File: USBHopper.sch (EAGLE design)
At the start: 38 parts, among them X1 USB-1X-2S-PLUG-A-SMD

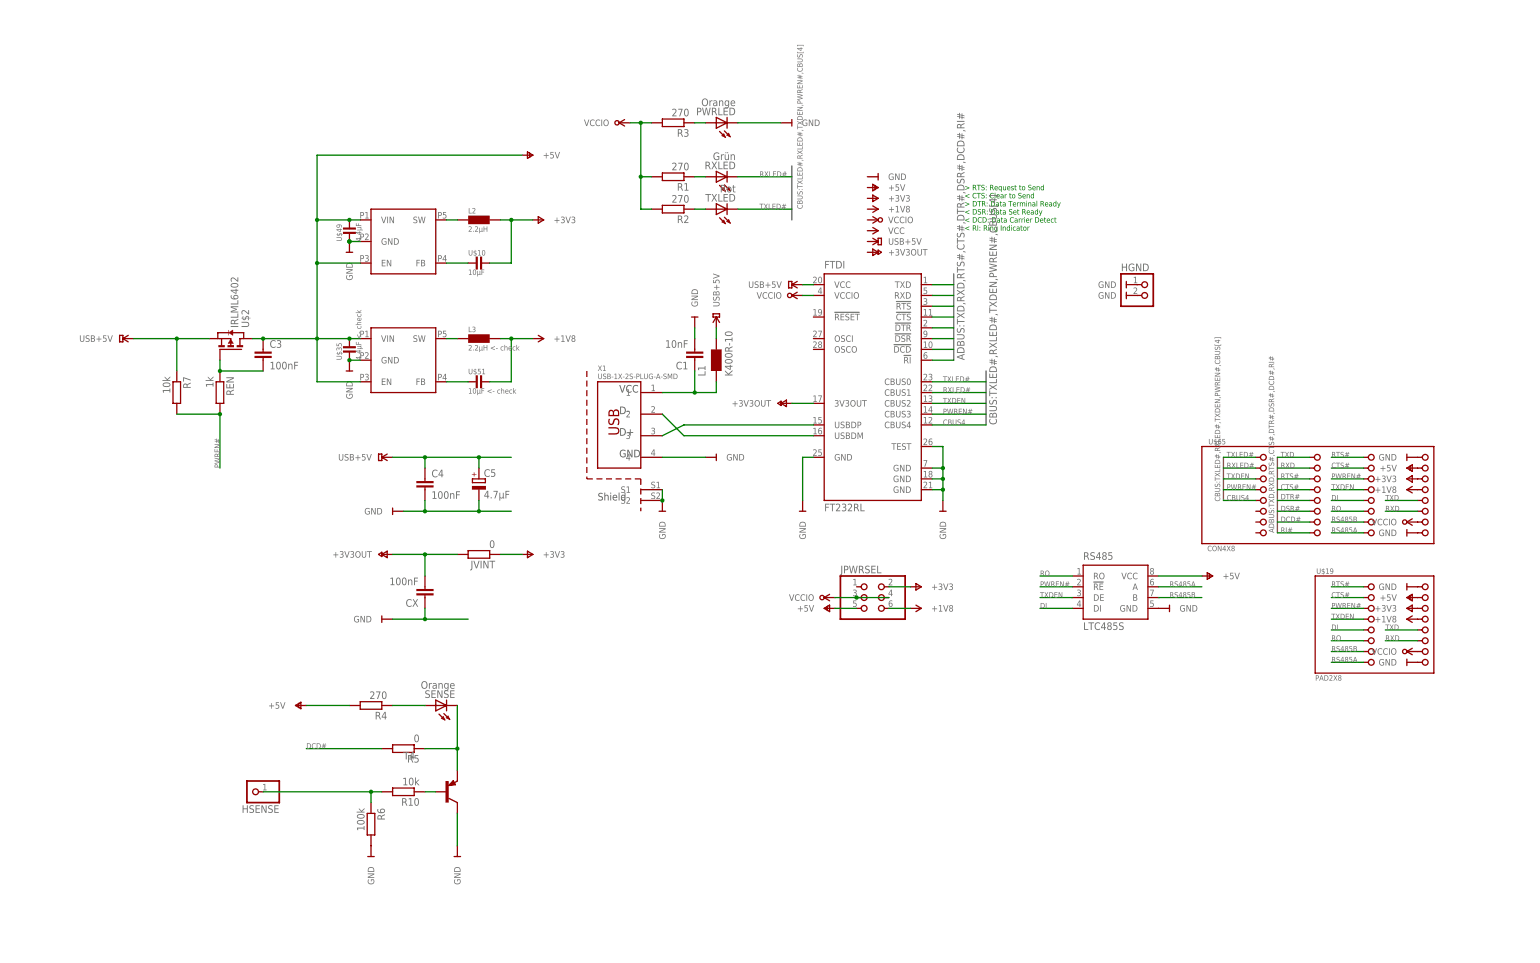
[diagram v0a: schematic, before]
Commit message: LED Steuerung via RN4904
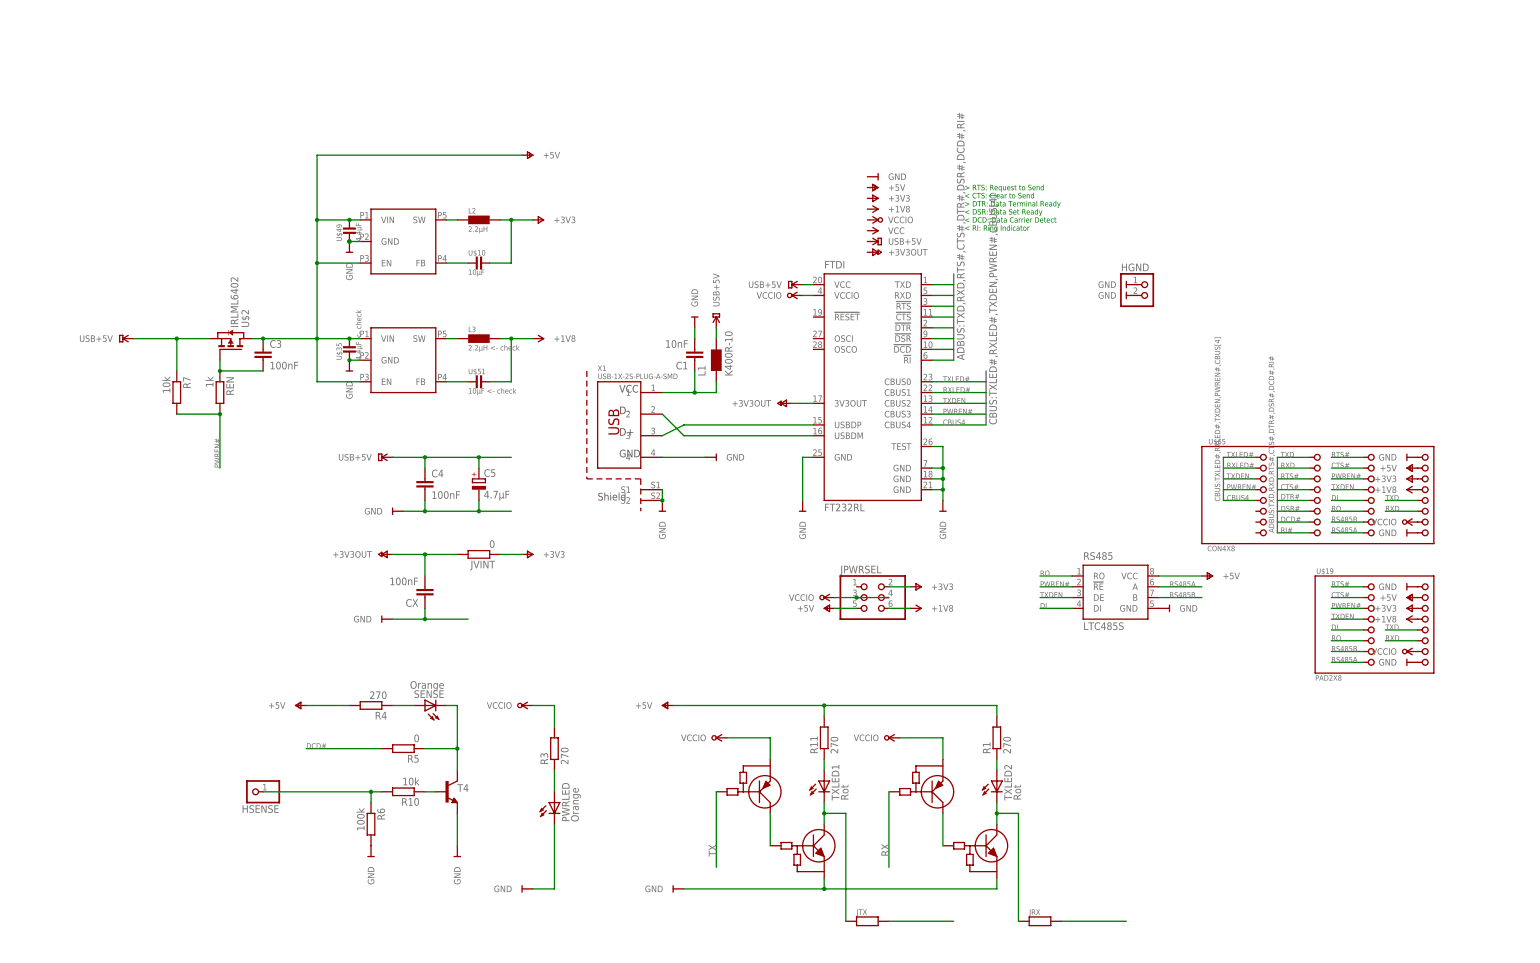
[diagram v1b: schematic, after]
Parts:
- removed R2: 270, rcl:R-EU_R0805
- removed RXLED: Grün, led:LEDCHIP-LED0805
- removed TXLED: Rot, led:LEDCHIP-LED0805
- added JRX, JTX: (no value), flo-parts:RESISTORCONNECT
- added R11: 270, rcl:R-EU_R0805
- added TXLED1, TXLED2: Rot, led:LEDCHIP-LED0805
- added U$32, U$46: (no value), flo-logic:RN4904
- T4: device transistor:BC857A-PNP-SOT23-BEC -> transistor:-NPN-SOT23-EBC
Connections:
- new net N$10: JTX.P$1, TXLED1.C, U$32NPN.E
- new net N$11: R11.1, TXLED1.A
- new net N$12: R1.1, TXLED2.A
- new net N$9: U$32NPN.B, U$32PNP.C
- new net RX: U$46PNP.B
- new net TX: U$32PNP.B
- net +5V: now also R1.2, R11.2
- net GND: now also T4.E, U$32NPN.C, U$46NPN.C; no longer T4.C
- net N$5: now also U$46NPN.B, U$46PNP.C; no longer R1.1, RXLED.A
- net N$6: now also JRX.P$1, TXLED2.C, U$46NPN.E; no longer R2.1, TXLED.A
- net RXLED#: now also JRX.P$2; no longer RXLED.C
- net SENSLED: now also T4.C; no longer T4.E
- net TXLED#: now also JTX.P$2; no longer TXLED.C
- net VCCIO: now also U$32PNP.E, U$46PNP.E; no longer R1.2, R2.2
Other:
- note added: "SIMPLE"
- note added: "integrated"
- moved on the sheet: PWRLED, R1, R3, SENSE

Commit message: pnp/npn package groesser. strom schaltung gefummele.
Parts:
- removed JVINT: 0, rcl:R-EU_R0805
- removed R10: 10k, rcl:R-EU_R0805
- removed R6: 100k, rcl:R-EU_R0805
- removed T4: (no value), transistor:-NPN-SOT23-EBC
- removed U$2: IRLML6402, IRLML6402:IRLML6402
- added IC1: (no value), ic-package:DIL8
- added JINT: (no value), flo-parts:RESISTORCONNECT
- added U$57: DMP2240UDM, flo-logic:DMP2240UDM
- added U$64, U$72: 4k7/47k, flo-logic:PNP_NPN_BIASNXP_PIMD3
- added U$73: (no value), flo-logic:PNP_NPN_BIASNXP_PIMD3
- U$32, U$46: value (none) -> CON1X4; device flo-logic:RN4904 -> flo-header:CON1X4
- renumbered TXLED1 to TXLED, TXLED2 to RXLED
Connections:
- removed net N$23: R10.1, T4.B
- net +3V3: now also JINT.P$2; no longer JVINT.1
- net +3V3OUT: now also JINT.P$1; no longer JVINT.2
- net +5V: now also U$32.P$1, U$57A.D; no longer U$2.D, U$20.EN, U$20.VIN, U$49.P$2
- net DI: now also U$46.P$4
- net GND: now also U$32.P$4, U$64NPN.C, U$72NPN.C, U$73NPN.C; no longer R6.2, T4.E, U$32NPN.C, U$46NPN.C
- net N$10: now also U$64NPN.E; no longer U$32NPN.E
- net N$5: now also U$72NPN.B, U$72PNP.C; no longer U$46NPN.B, U$46PNP.C
- net N$6: now also U$72NPN.E; no longer U$46NPN.E
- net N$9: now also U$64NPN.B, U$64PNP.C; no longer U$32NPN.B, U$32PNP.C
- net PWREN: now also U$57A.G; no longer U$2.G
- net PWREN#: now also U$46.P$2
- net RO: now also U$46.P$1
- net RS485A: now also U$32.P$2
- net RS485B: now also U$32.P$3
- net RX: now also U$72PNP.B; no longer U$46PNP.B
- net SENSE: now also U$73NPN.B; no longer R10.2, R6.1
- net SENSLED: now also U$73NPN.E; no longer T4.C
- net TX: now also U$64PNP.B; no longer U$32PNP.B
- net TXDEN: now also U$46.P$3
- net USB+5V: now also U$20.EN, U$20.VIN, U$49.P$2, U$57A.S; no longer U$2.S
- net VCCIO: now also U$64PNP.E, U$72PNP.E; no longer U$32PNP.E, U$46PNP.E
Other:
- moved on the sheet: C3, PWRLED, R3, R7, REN

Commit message: weiter pwren, leds...
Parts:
- removed IC1: (no value), ic-package:DIL8
- removed JINT: (no value), flo-parts:RESISTORCONNECT
- removed R5: 0, rcl:R-EU_R0805
- added JP1, JP2: (no value), pinhead:PINHD-1X1
- C5: device rcl:CPOL-EUB -> rcl:CPOL-EU153CLV-0405
- PWRLED: value Orange -> Blue
- RXLED: value Rot -> Red
- TXLED: value Rot -> Green
- renumbered R1 to RRX, R11 to RTX, U$64 to UTX, U$72 to URX
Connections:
- new net N$13: R3.2, U$73PNP.C
- new net N$14: JP1.1, U$73PNP.B
- net +3V3: no longer JINT.P$2
- net +3V3OUT: now also JPWRSEL.1; no longer JINT.P$1
- net +5V: now also U$20.EN, U$20.VIN, U$49.P$2
- net DCD#: no longer R5.2
- net PWREN#: now also JP2.1
- net SENSLED: no longer R5.1
- net USB+5V: now also U$73PNP.E; no longer U$20.EN, U$20.VIN, U$49.P$2
- net VCCIO: no longer R3.2
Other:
- note removed: "SIMPLE"
- note removed: "integrated"
- moved on the sheet: HSENSE, PWRLED, R3, R4, SENSE, U$73NPN

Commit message: +5V->USB+5V bei sense
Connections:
- net +5V: no longer R4.2
- net USB+5V: now also R4.2
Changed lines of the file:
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@@
 <part name="HSENSE" library="pinhead" deviceset="PINHD-1X1" device=""/>
 <part name="R4" library="rcl" deviceset="R-EU_" device="R0805" value="270"/>
-<part name="U$54" library="supply3" deviceset="+5V" device=""/>
 <part name="U$55" library="supply3" deviceset="GND" device=""/>
 <part name="U$3" library="supply3" deviceset="+5V" device=""/>
@@
 <part name="JP1" library="pinhead" deviceset="PINHD-1X1" device=""/>
 <part name="JP2" library="pinhead" deviceset="PINHD-1X1" device=""/>
+<part name="U$38" library="supply3" deviceset="USB+5V" device=""/>
 </parts>
 <sheets>
@@
 <instance part="HSENSE" gate="G$1" x="-81.28" y="-50.8" rot="R180"/>
 <instance part="R4" gate="G$1" x="-53.34" y="-27.94" rot="R90"/>
-<instance part="U$54" gate="G$1" x="-68.58" y="-20.32" rot="R180"/>
 <instance part="U$55" gate="G$1" x="-68.58" y="-66.04" rot="R180"/>
 <instance part="U$3" gate="G$1" x="157.48" y="7.62"/>
@@
 <instance part="JP1" gate="G$1" x="-17.78" y="-35.56" rot="R180"/>
 <instance part="JP2" gate="G$1" x="-20.32" y="-35.56"/>
+<instance part="U$38" gate="G$1" x="-68.58" y="-20.32" rot="R180"/>
 </instances>
 <busses>
@@
 <pinref part="U$33" gate="G$1" pin="USB+5V"/>
 </segment>
+<segment>
+<pinref part="R4" gate="G$1" pin="2"/>
+<wire x1="-66.04" y1="-20.32" x2="-53.34" y2="-20.32" width="0.1524" layer="91"/>
+<wire x1="-53.34" y1="-20.32" x2="-53.34" y2="-22.86" width="0.1524" layer="91"/>
+<pinref part="U$38" gate="G$1" pin="USB+5V"/>
+</segment>
 </net>
 <net name="+3V3OUT" class="0">
@@
 <net name="+5V" class="0">
 <segment>
-<pinref part="U$54" gate="G$1" pin="+5V"/>
-<pinref part="R4" gate="G$1" pin="2"/>
-<wire x1="-66.04" y1="-20.32" x2="-53.34" y2="-20.32" width="0.1524" layer="91"/>
-<wire x1="-53.34" y1="-20.32" x2="-53.34" y2="-22.86" width="0.1524" layer="91"/>
-</segment>
-<segment>
 <pinref part="RS485" gate="G$1" pin="VCC"/>

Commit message: Viel Layout
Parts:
- removed C1: 10nF, rcl:C-EUC0805
- removed C3: 100nF, rcl:C-EUC0805
- removed HSENSE, JP1, JP2: (no value), pinhead:PINHD-1X1
- removed U$46: CON1X4, flo-header:CON1X4
- added C2: 10nF, flo-parts:CAPACITOR
- added Q1: 2.5A/30V, SparkFun-DiscreteSemi:MOSFET-PCHANNELDMG2307L
- added U$21: CON1X1PIN_XL, flo-header:CON1X1PIN_XL
- added U$27: CON1X2PIN_BRIDGE, flo-header:CON1X2PIN_BRIDGE
- added U$64: CON1X8PIN_L, flo-header:CON1X8PIN_L
- added U$66: PAD2X8PADS, flo-header:PAD2X8PADS
- added U$76: CON2X8, flo-header:CON2X8
- C4, CX: device rcl:C-EUC0805 -> flo-parts:CAPACITOR
- R3, R4, R7, REN, RRX, RTX: device rcl:R-EU_R0805 -> flo-parts:RESISTORWIDE
- U$19: value PAD2X8 -> CON2X2PIN_L; device flo-header:PAD2X8 -> flo-header:CON2X2PIN_L
- U$32: value CON1X4 -> 100nF; device flo-header:CON1X4 -> flo-parts:CAPACITOR
- U$57: value DMP2240UDM -> IC8DIL; device flo-logic:DMP2240UDM -> flo-gen-ic:IC8DIL
- U$65: value CON4X8 -> PAD2X8PIN_L; device flo-header:CON4X8 -> flo-header:PAD2X8PIN_L
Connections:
- removed net FB: U$11.FB, U$51.P$1
- removed net SW: L3.P$2, U$11.SW
- net +1V8: now also U$11.SW, U$64.P$4, U$66.P$7; no longer U$19.P$8, U$65.P$16
- net +3V3: now also U$10.P$1, U$20.SW, U$64.P$3, U$66.P$5; no longer U$10.P$2, U$19.P$6, U$65.P$12
- net +3V3OUT: now also CX.P$2; no longer CX.2
- net +5V: now also Q1.D, RRX.P$2, RTX.P$2, U$32.P$2, U$57.P$8, U$64.P$2, U$66.P$3; no longer C3.1, RRX.2, RTX.2, U$19.P$4, U$32.P$1, U$57A.D, U$65.P$8
- net CBUS4: now also U$65.P$13; no longer U$65.P$17
- net CTS#: now also U$65.P$4, U$66.P$4; no longer U$19.P$3, U$65.P$14, U$65.P$7
- net DCD#: now also U$65.P$7; no longer U$65.P$26
- net DI: now also U$19.P$4, U$57.P$4; no longer U$19.P$9, U$46.P$4, U$65.P$19
- net DSR#: now also U$65.P$6; no longer U$65.P$22
- net DTR#: now also U$65.P$5; no longer U$65.P$18
- net GND: now also C2.P$2, C4.P$1, CX.P$1, U$10.P$2, U$51.P$1, U$57.P$5, U$64.P$1, U$64.P$8, U$65.P$14, U$66.P$1, U$66.P$15; no longer C1.2, C4.2, CX.1, U$19.P$16, U$19.P$2, U$32.P$4, U$65.P$32, U$65.P$4
- net N$1: now also R3.P$1; no longer R3.1
- net N$11: now also RTX.P$1; no longer RTX.1
- net N$12: now also RRX.P$1; no longer RRX.1
- net N$13: now also R3.P$2; no longer R3.2
- net N$14: now also U$27.P$1; no longer JP1.1
- net N$2: now also R4.P$1; no longer R4.1
- net N$4: now also C2.P$1; no longer C1.1
- net N$7: now also L3.P$2, U$11.FB; no longer L2.P$2, U$20.SW
- net N$8: now also L2.P$2; no longer U$10.P$1
- net PWREN: now also Q1.G, REN.P$2, U$32.P$1; no longer C3.2, REN.1, U$57A.G
- net PWREN#: now also R7.P$1, REN.P$1, U$27.P$2, U$57.P$2, U$65.P$12, U$66.P$6; no longer JP2.1, R7.2, REN.2, U$19.P$5, U$46.P$2, U$65.P$11, U$65.P$13
- net RI#: now also U$65.P$8; no longer U$65.P$30
- net RO: now also U$19.P$2, U$57.P$1; no longer U$19.P$11, U$46.P$1, U$65.P$23
- net RS485A: now also U$57.P$6, U$65.P$15, U$66.P$16; no longer U$19.P$15, U$32.P$2, U$65.P$31
- net RS485B: now also U$57.P$7, U$65.P$16, U$66.P$14; no longer U$19.P$13, U$32.P$3, U$65.P$27
- net RTS#: now also U$66.P$2; no longer U$19.P$1, U$65.P$10
- net RXD: now also U$19.P$1, U$64.P$6, U$65.P$2, U$66.P$11; no longer U$19.P$12, U$65.P$24, U$65.P$6
- net RXLED#: now also U$65.P$10; no longer U$65.P$5
- net SENSE: now also U$21.P$1; no longer HSENSE.1
- net TXD: now also U$19.P$3, U$64.P$5, U$65.P$1, U$66.P$9; no longer U$19.P$10, U$65.P$2, U$65.P$20
- net TXDEN: now also U$57.P$3, U$65.P$11, U$66.P$8; no longer U$19.P$7, U$46.P$3, U$65.P$15, U$65.P$9
- net TXLED#: now also U$65.P$9; no longer U$65.P$1
- net USB+5V: now also C4.P$2, Q1.S, R4.P$2, R7.P$2; no longer C4.1, R4.2, R7.1, U$57A.S
- net VCCIO: now also U$64.P$7, U$66.P$13; no longer U$19.P$14, U$65.P$28
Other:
- moved on the sheet: HGND, L2, L3, RS485, U$10, U$51

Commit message: Layout fertig. Logo!
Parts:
- removed CX, U$32: 100nF, flo-parts:CAPACITOR
- removed U$76: CON2X8, flo-header:CON2X8
- added C1: 10nF, flo-parts:CAPACITOR
- added C3: 100nF, flo-parts:CAPACITOR
- C2: value 10nF -> 100nF
- L1: device wuerth-elektronik:WE-CBF_0805 -> wuerth_elektronik:WE-CBF_0805
- PWRLED, RXLED, SENSE, TXLED: device led:LEDCHIP-LED0805 -> flo-led:LEDKPT-2012
- U$27: value CON1X2PIN_BRIDGE -> CON1X2PIN_XL; device flo-header:CON1X2PIN_BRIDGE -> flo-header:CON1X2PIN_XL
- renumbered R7 to R1, REN to R2, RRX to R6, RTX to R5, U$10 to C8, U$11 to U5, U$20 to U4, U$35 to C7, U$49 to C6, U$51 to C9, U$73 to U1, URX to U3, UTX to U2
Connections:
- net N$5 renamed U3
- net +3V3OUT: now also C4.P$2; no longer CX.P$2
- net +5V: now also C2.P$2; no longer U$32.P$2
- net GND: now also C1.P$2, C3.P$1; no longer C2.P$2, CX.P$1
- net N$1: now also R4.P$1; no longer R3.P$1
- net N$13: now also R4.P$2; no longer R3.P$2
- net N$2: now also R3.P$1; no longer R4.P$1
- net N$4: now also C1.P$1; no longer C2.P$1
- net PWREN: now also C2.P$1; no longer U$32.P$1
- net USB+5V: now also C3.P$2, R3.P$2; no longer C4.P$2, R4.P$2
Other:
- moved on the sheet: C2, C4, R3, R4

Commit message: LED beschriftungen
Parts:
- renumbered PWRLED to LED2, RXLED to LED3, SENSE to LED1, TXLED to LED4
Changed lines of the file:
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@@
 <part name="U$24" library="supply3" deviceset="GND" device=""/>
 <part name="U$50" library="supply3" deviceset="+5V" device=""/>
-<part name="PWRLED" library="flo-led" deviceset="LED" device="KPT-2012" value="Blue"/>
+<part name="LED2" library="flo-led" deviceset="LED" device="KPT-2012" value="Blue"/>
 <part name="U$52" library="supply3" deviceset="GND" device=""/>
 <part name="HGND" library="pinhead" deviceset="PINHD-1X2" device=""/>
@@
 <part name="U$56" library="supply3" deviceset="GND" device=""/>
 <part name="U$58" library="supply3" deviceset="GND" device=""/>
-<part name="SENSE" library="flo-led" deviceset="LED" device="KPT-2012" value="Orange"/>
+<part name="LED1" library="flo-led" deviceset="LED" device="KPT-2012" value="Orange"/>
 <part name="U4" library="flo-parts" deviceset="DCDC" device=""/>
 <part name="U5" library="flo-parts" deviceset="DCDC" device=""/>
-<part name="TXLED" library="flo-led" deviceset="LED" device="KPT-2012" value="Green"/>
+<part name="LED4" library="flo-led" deviceset="LED" device="KPT-2012" value="Green"/>
 <part name="U$48" library="supply3" deviceset="+5V" device=""/>
 <part name="U$59" library="supply3" deviceset="VCCIO" device=""/>
 <part name="U$60" library="supply3" deviceset="GND" device=""/>
-<part name="RXLED" library="flo-led" deviceset="LED" device="KPT-2012" value="Red"/>
+<part name="LED3" library="flo-led" deviceset="LED" device="KPT-2012" value="Red"/>
 <part name="U$61" library="supply3" deviceset="VCCIO" device=""/>
 <part name="JTX" library="flo-parts" deviceset="RESISTOR" device="CONNECT"/>
@@
 <instance part="U$24" gate="G$1" x="35.56" y="68.58" rot="R90"/>
 <instance part="U$50" gate="G$1" x="0" y="106.68"/>
-<instance part="PWRLED" gate="G$1" x="0" y="-60.96" rot="R270"/>
+<instance part="LED2" gate="G$1" x="0" y="-60.96" rot="R270"/>
 <instance part="U$52" gate="G$1" x="-15.24" y="-66.04" rot="R180"/>
 <instance part="HGND" gate="G$1" x="35.56" y="0"/>
@@
 <instance part="U$56" gate="G$1" x="-45.72" y="83.82" rot="R270"/>
 <instance part="U$58" gate="G$1" x="-45.72" y="55.88" rot="R270"/>
-<instance part="SENSE" gate="G$1" x="-53.34" y="-40.64" rot="R270"/>
+<instance part="LED1" gate="G$1" x="-53.34" y="-40.64" rot="R270"/>
 <instance part="U4" gate="G$1" x="-33.02" y="86.36"/>
 <instance part="U5" gate="G$1" x="-33.02" y="58.42"/>
-<instance part="TXLED" gate="G$1" x="66.04" y="-43.18" rot="R270"/>
+<instance part="LED4" gate="G$1" x="66.04" y="-43.18" rot="R270"/>
 <instance part="U$48" gate="G$1" x="27.94" y="-22.86" rot="MR0"/>
 <instance part="U$59" gate="G$1" x="40.64" y="-30.48" rot="R180"/>
 <instance part="U$60" gate="G$1" x="30.48" y="-66.04" rot="R180"/>
-<instance part="RXLED" gate="G$1" x="106.68" y="-43.18" rot="R270"/>
+<instance part="LED3" gate="G$1" x="106.68" y="-43.18" rot="R270"/>
 <instance part="U$61" gate="G$1" x="81.28" y="-30.48" rot="R180"/>
 <instance part="JTX" gate="R$1" x="76.2" y="-73.66"/>
@@
 <wire x1="0" y1="-63.5" x2="0" y2="-66.04" width="0.1524" layer="91"/>
 <wire x1="0" y1="-66.04" x2="-12.7" y2="-66.04" width="0.1524" layer="91"/>
-<pinref part="PWRLED" gate="G$1" pin="C"/>
+<pinref part="LED2" gate="G$1" pin="C"/>
 </segment>
 <segment>
@@
 <net name="N$1" class="0">
 <segment>
-<pinref part="PWRLED" gate="G$1" pin="A"/>
+<pinref part="LED2" gate="G$1" pin="A"/>
 <wire x1="0" y1="-53.34" x2="0" y2="-55.88" width="0.1524" layer="91"/>
 <pinref part="R4" gate="R$1" pin="P$1"/>
@@
 <segment>
 <wire x1="-53.34" y1="-33.02" x2="-53.34" y2="-35.56" width="0.1524" layer="91"/>
-<pinref part="SENSE" gate="G$1" pin="A"/>
+<pinref part="LED1" gate="G$1" pin="A"/>
 <pinref part="R3" gate="R$1" pin="P$1"/>
 </segment>
@@
 <segment>
 <wire x1="-53.34" y1="-43.18" x2="-53.34" y2="-45.72" width="0.1524" layer="91"/>
-<pinref part="SENSE" gate="G$1" pin="C"/>
+<pinref part="LED1" gate="G$1" pin="C"/>
 <pinref part="U1" gate="NPN" pin="E"/>
 </segment>
@@
 <net name="N$10" class="0">
 <segment>
-<pinref part="TXLED" gate="G$1" pin="C"/>
+<pinref part="LED4" gate="G$1" pin="C"/>
 <wire x1="66.04" y1="-50.8" x2="66.04" y2="-48.26" width="0.1524" layer="91"/>
 <pinref part="JTX" gate="R$1" pin="P$1"/>
@@
 <net name="N$11" class="0">
 <segment>
-<pinref part="TXLED" gate="G$1" pin="A"/>
+<pinref part="LED4" gate="G$1" pin="A"/>
 <wire x1="66.04" y1="-38.1" x2="66.04" y2="-35.56" width="0.1524" layer="91"/>
 <pinref part="R5" gate="R$1" pin="P$1"/>
@@
 <net name="N$6" class="0">
 <segment>
-<pinref part="RXLED" gate="G$1" pin="C"/>
+<pinref part="LED3" gate="G$1" pin="C"/>
 <wire x1="106.68" y1="-50.8" x2="106.68" y2="-48.26" width="0.1524" layer="91"/>
 <pinref part="JRX" gate="R$1" pin="P$1"/>
@@
 <net name="N$12" class="0">
 <segment>
-<pinref part="RXLED" gate="G$1" pin="A"/>
+<pinref part="LED3" gate="G$1" pin="A"/>
 <wire x1="106.68" y1="-38.1" x2="106.68" y2="-35.56" width="0.1524" layer="91"/>
 <pinref part="R6" gate="R$1" pin="P$1"/>
